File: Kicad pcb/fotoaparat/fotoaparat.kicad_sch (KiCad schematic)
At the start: 75 parts, among them IC1 Lineární Regulátor, IC3 Lineární Regulátor Displaye, J1 USB Konektor, J2 SWD, J3 LCD konektor, J4 Baterie, J5 GSD090012SEU, J6 UART, J7 Kamera, J9 Conn_01x11_Socket, U1 STM32L496RETx, U2 MCP73833-FCI/UN, Y1 8mhz krystal

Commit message: Oprava chyb
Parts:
- removed C13, C19, C20, C8: 1u, Capacitor_SMD:C_0805_2012Metric_Pad1.18x1.45mm_HandSolder, symbol Device:C
- added C22: 1u, Capacitor_SMD:C_0805_2012Metric_Pad1.18x1.45mm_HandSolder, symbol Device:C
- C7: value 1u -> 10u; footprint Capacitor_SMD:C_0805_2012Metric_Pad1.18x1.45mm_HandSolder -> Capacitor_THT:CP_Radial_D5.0mm_P2.50mm
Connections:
- net +3.3V: now also C22.2
- net GND: now also C22.1

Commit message: Připraveno na výrobu
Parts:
- added C8: 10u, Capacitor_THT:CP_Radial_D5.0mm_P2.50mm, symbol Device:C
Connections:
- net +3.3V: now also C8.1
- net GND: now also C8.2
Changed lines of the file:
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@@
 	)
 	(junction
+		(at 106.68 109.22)
+		(diameter 0)
+		(color 0 0 0 0)
+	)
+	(junction
 		(at 213.36 59.69)
 		(diameter 0)
@@
 	(wire
 		(pts
+			(xy 114.3 109.22) (xy 114.3 111.76)
+		)
+		(stroke
+			(width 0)
+			(type default)
+		)
+	)
+	(wire
+		(pts
 			(xy 207.01 20.32) (xy 207.01 19.05)
 		)
@@
 	(symbol
 		(lib_id "Device:C")
+		(at 110.49 109.22 90)
+		(unit 1)
+		(exclude_from_sim no)
+		(in_bom yes)
+		(on_board yes)
+		(dnp no)
+		(fields_autoplaced yes)
+		(property "Reference" "C8"
+			(at 110.49 101.6 90)
+			(effects
+				(font
+					(size 1.27 1.27)
+				)
+			)
+		)
+		(property "Value" "10u"
+			(at 110.49 104.14 90)
+			(effects
+				(font
+					(size 1.27 1.27)
+				)
+			)
+		)
+		(property "Footprint" "Capacitor_THT:CP_Radial_D5.0mm_P2.50mm"
+			(at 114.3 108.2548 0)
+			(effects
+				(font
+					(size 1.27 1.27)
+				)
+				(hide yes)
+			)
+		)
+		(property "Datasheet" "~"
+			(at 110.49 109.22 0)
+			(effects
+				(font
+					(size 1.27 1.27)
+				)
+				(hide yes)
+			)
+		)
+		(property "Description" "Unpolarized capacitor"
+			(at 110.49 109.22 0)
+			(effects
+				(font
+					(size 1.27 1.27)
+				)
+				(hide yes)
+			)
+		)
+		(pin "1"
+		)
+		(pin "2"
+		)
+		(instances
+			(project ""
+				(path "/af31909f-b2e8-4f24-bd61-08599f2fc290"
+					(reference "C8")
+					(unit 1)
+				)
+			)
+		)
+	)
+	(symbol
+		(lib_id "Device:C")
 		(at -77.47 172.72 270)
 		(unit 1)
@@
 					(unit 1)
 				)
+			)
+		)
+	)
+	(symbol
+		(lib_id "power:GND")
+		(at 114.3 111.76 0)
+		(unit 1)
+		(exclude_from_sim no)
+		(in_bom yes)
+		(on_board yes)
+		(dnp no)
+		(fields_autoplaced yes)
+		(property "Reference" "#PWR050"
+			(at 114.3 118.11 0)
+			(effects
+				(font
+					(size 1.27 1.27)
+				)
+				(hide yes)
+			)
+		)
+		(property "Value" "GND"
+			(at 114.3 116.84 0)
+			(effects
+				(font
+					(size 1.27 1.27)
+				)
+			)
+		)
+		(property "Footprint" ""
+			(at 114.3 111.76 0)
+			(effects
+				(font
+					(size 1.27 1.27)
+				)
+				(hide yes)
+			)
+		)
+		(property "Datasheet" ""
+			(at 114.3 111.76 0)
+			(effects
+				(font
+					(size 1.27 1.27)
+				)
+				(hide yes)
+			)
+		)
+		(property "Description" "Power symbol creates a global label with name \"GND\" , ground"
+			(at 114.3 111.76 0)
+			(effects
+				(font
+					(size 1.27 1.27)
+				)
+				(hide yes)
+			)
+		)
+		(pin "1"
+		)
+		(instances
+			(project ""
+				(path "/af31909f-b2e8-4f24-bd61-08599f2fc290"
+					(reference "#PWR050")
+					(unit 1)
+				)

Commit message: Úprava designu
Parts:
- removed C10, C11, C12, C14, C21, C9: 100n, Capacitor_SMD:C_0805_2012Metric_Pad1.18x1.45mm_HandSolder, symbol Device:C
- removed C15, C16, C22: 1u, Capacitor_SMD:C_0805_2012Metric_Pad1.18x1.45mm_HandSolder, symbol Device:C
- removed C17, C18: 30p, Capacitor_SMD:C_0805_2012Metric_Pad1.18x1.45mm_HandSolder, symbol Device:C
- removed C7, C8: 10u, Capacitor_THT:CP_Radial_D5.0mm_P2.50mm, symbol Device:C
- removed D1, D2, D3: LED, LED_SMD:LED_0805_2012Metric_Pad1.15x1.40mm_HandSolder, symbol Device:LED
- removed FB1: 120R, Inductor_SMD:L_0805_2012Metric_Pad1.05x1.20mm_HandSolder, symbol Device:FerriteBead
- removed H1, H2, H3, H4: MountingHole, MountingHole:MountingHole_3.2mm_M3, symbol Mechanical:MountingHole
- removed IC1: Lineární Regulátor, Package_TO_SOT_SMD:TSOT-23-5_HandSoldering, symbol NCP718ASN330T1G:NCP718ASN330T1G
- removed IC3: Lineární Regulátor Displaye, Package_TO_SOT_SMD:TSOT-23-5_HandSoldering, symbol NCP718ASN330T1G:NCP718ASN330T1G
- removed J1: USB Konektor, 47436:473460001, symbol 47346-0001:47346-0001
- removed J2: SWD, Connector_PinHeader_2.54mm:PinHeader_1x04_P2.54mm_Vertical, symbol Connector:Conn_01x04_Socket
- removed J3: LCD konektor, FFC2A32-20-T:GCT_FFC2A32-20-T, symbol FFC2A32-20-T:FFC2A32-20-T
- removed J4: Baterie, Connector_PinSocket_2.54mm:PinSocket_1x02_P2.54mm_Horizontal, symbol Connector:Conn_01x02_Socket
- removed J5: GSD090012SEU, gsd09:GSD090012SEU_AMP, symbol 2025-09-30_19-14-30:GSD090012SEU
- removed J6: UART, Connector_PinHeader_2.54mm:PinHeader_1x02_P2.54mm_Vertical, symbol Connector:Conn_01x02_Socket
- removed J7: Kamera, Connector_PinSocket_2.54mm:PinSocket_2x11_P2.54mm_Vertical, symbol Connector_Generic:Conn_02x11_Odd_Even
- removed J9: Conn_01x11_Socket, Connector_PinSocket_2.54mm:PinSocket_1x11_P2.54mm_Horizontal, symbol Connector:Conn_01x11_Socket
- removed R10, R11, R12, R13, R14, R15, R16, R17, R18, R19, R20, R21, R22, R23, R24, R26, R9: 4.7k, Resistor_SMD:R_0805_2012Metric_Pad1.20x1.40mm_HandSolder, symbol Device:R
- removed R25, R7: 1k, Resistor_SMD:R_0805_2012Metric_Pad1.20x1.40mm_HandSolder, symbol Device:R
- removed R8: 2, Resistor_SMD:R_0805_2012Metric_Pad1.20x1.40mm_HandSolder, symbol Device:R
- removed S1: Zapínací spínač, mfs:MFS201N24Z, symbol MFS201N-24-Z:MFS201N-24-Z
- removed S2: tlačítko doleva, mc3:MC32829, symbol MC32829:MC32829
- removed S3: prostřední tlačítko, mc3:MC32829, symbol MC32829:MC32829
- removed S4: tlačítko doprava, mc3:MC32829, symbol MC32829:MC32829
- removed S5: spínač, cfs201mb:CFS0201MB, symbol CFS-0201MB:CFS-0201MB
- removed TH1: 10k, Connector_PinSocket_2.54mm:PinSocket_1x02_P2.54mm_Horizontal, symbol Device:Thermistor
- removed U1: STM32L496RETx, Package_QFP:LQFP-64_10x10mm_P0.5mm, symbol MCU_ST_STM32L4:STM32L496RETx
- removed U2: MCP73833-FCI/UN, MCP:MSOP10_MC_MCH, symbol 2025-09-30_17-20-56:MCP73833-FCI_UN
- removed Y1: 8mhz krystal, hc4:HC49S830507030ATF, symbol HC49S-8-30-50-70-30-ATF:HC49S-8-30-50-70-30-ATF
- added J1: Conn_02x01, Connector_PinHeader_2.54mm:PinHeader_2x01_P2.54mm_Vertical, symbol Connector_Generic:Conn_02x01
- added Q1, Q2: BC547, Package_TO_SOT_THT:TO-92_Inline, symbol Transistor_BJT:BC547
- added SW1: SW_Push_Dual, Tlačítko:tlačítko 6x6x12, symbol Switch:SW_Push_Dual
- added U1: TP4056, TP4056:TP4056, symbol tp4056:tp4056
- added U2: ov7670 fifo, ov7670:ov7670, symbol ov7670:ov7670
- added U3: Stm32 Bluepill, Stm32 Bluepill:Bluepill, symbol Stm32 Bluepill:Stm32_Bluepill
- added U4: Lcd Display, Lcd Display:ili9341, symbol ili9341:lcd_ili9341
- added U5: FJ08k, Tlačítko:FJ08K-S, symbol Joystick FJ08K:FJ08k
- added U6, U8, U9: Me6211c, Package_TO_SOT_SMD:SOT-23-5, symbol Me6211c:Me6211c
- added U7: VBsemi SI2312CDS-T1-GE3, Package_TO_SOT_SMD:SOT-23W_Handsoldering, symbol Mosfet N:Mosfet_N
- BZ1: footprint Inductor_SMD:L_SXN_SMDRI73 -> Jiangsu:Jiangsu
- C1, C2, C3, C4, C5, C6: value 1u -> 4.7uf
- R1, R2: value 4.7k -> 100k; footprint Resistor_SMD:R_0805_2012Metric_Pad1.20x1.40mm_HandSolder -> Resistor_THT:R_Axial_DIN0207_L6.3mm_D2.5mm_P10.16mm_Horizontal
- R3: value 4.7k -> 10k; footprint Resistor_SMD:R_0805_2012Metric_Pad1.20x1.40mm_HandSolder -> Resistor_THT:R_Axial_DIN0207_L6.3mm_D2.5mm_P10.16mm_Horizontal
- R4: value 1k -> 100k; footprint Resistor_SMD:R_0805_2012Metric_Pad1.20x1.40mm_HandSolder -> Resistor_THT:R_Axial_DIN0207_L6.3mm_D2.5mm_P10.16mm_Horizontal
- R5: value 1k -> 30k; footprint Resistor_SMD:R_0805_2012Metric_Pad1.20x1.40mm_HandSolder -> Resistor_THT:R_Axial_DIN0207_L6.3mm_D2.5mm_P10.16mm_Horizontal
- R6: value 1k -> 50k; footprint Resistor_SMD:R_0805_2012Metric_Pad1.20x1.40mm_HandSolder -> Resistor_THT:R_Axial_DIN0207_L6.3mm_D2.5mm_P10.16mm_Horizontal
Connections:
- net +3.3V LCD is gone; now on net GND: C6.2
- net buzzer is gone; now on net +BATT: BZ1.1 (+)
- net sw2 is gone; now on an unnamed net: R2.2
- net +3.3V: now also C2.1, SW1.2, U3.23 (3v3), U5.1 (Y1), U5.4 (X1), U6.5 (Vout); no longer C4.2, R1.1, R2.1, R3.1
- net +BATT: now also R5.2, U1.5 (Bat+); no longer C2.1, C3.1, C5.1
- net GND: now also C4.2, R2.1, R3.1, R4.1, Q1.3 (E), Q2.3 (E), U1.4 (OUT-), U2.2 (gnd), U2.20 (oe), U3.19 (gnd), U3.21 (gnd), U3.22 (gnd), U4.13 (gnd), U5.2 (gnd), U5.5 (gnd), U6.2 (Vss), U6.4 (NC), U8.2 (Vss), U8.4 (NC), U9.2 (Vss), U9.4 (NC); no longer BZ1.2 (-), C4.1, C6.1
- net at R5.1: now also R4.2, U3.35 (pa1)
- net at R6.2: now also U3.9 (pa12)
- net Indikátor Nabíjení: no longer names the net of R6.1
- net Indikátor Nabíjení: now also Q1.2 (B), SW1.3
- net VBUS renamed +4V
- net +4V: now also C3.1, C5.1, U6.1 (Vin), U6.3 (CE), U7.3 (Drain), U8.1 (Vin), U8.3 (CE), U9.1 (Vin), U9.3 (CE)
- net sw1 renamed tx
- net tx: now also J1.1 (Pin_1), SW1.1, U3.6 (pa9)
- net sw3: no longer names the net of R1.2
- net sw3: now also SW1.4, U1.3 (OUT+), U7.2 (Source_gnd)
- new net: BZ1.2 (-), Q2.1 (C)
- new net: Q2.2 (B), U3.5 (pa8)
- new net: U3.28 (pb0), U4.10 (Dc)
- new net: U3.27 (pb1), U4.11 (Reset)
- new net: U3.32 (pa4), U4.12 (Cs)
- new net: U3.31 (pa5), U4.15 (sd_sck), U4.5 (T_clk), U4.8 (sck)
- new net: U3.30 (pa6), U4.16 (sd_miso), U4.2 (T_do), U4.6 (Sdo_miso)
- new net: U3.29 (pa7), U4.17 (sd_mosi), U4.3 (T_Din), U4.9 (sdi_mosi)
- new net: U3.1 (pb12), U4.18 (sd_cs)
- new net: U3.8 (pa11), U4.4 (T_cs)
- new net: U2.19 (wr), U3.10 (pa15)
- new net: U2.7 (d7), U3.11 (pb3)
- new net: U2.9 (d5), U3.12 (pb4)
- new net: U2.11 (d3), U3.13 (pb5)
- new net: U2.3 (sioc), U3.14 (pb6)
- new net: U2.4 (siod), U3.15 (pb7)
- new net: U2.13 (d1), U3.16 (pb8)
- new net: U2.8 (d6), U3.17 (pb9)
- new net: U2.14 (d0), U3.2 (pb13)
- new net: U2.10 (d4), U3.25 (pb11)
- new net: U2.12 (d2), U3.26 (pb10)
- new net: U2.18 (rck), U3.3 (pb14)
- new net: U3.33 (pa3), U5.6 (X2)
- new net: U3.34 (pa2), U5.3 (Y2)
- new net: U2.5 (vsync), U3.36 (pa0)
- new net: U2.22 (rrst), U3.4 (pb15)
- new net: Q1.1 (C), R1.1, U7.1 (Gate)
- new net +3.3V lcd: C6.1, U4.14 (Vcc), U4.7 (Led_3.3v), U9.5 (Vout)
- new net +3.3V ov7670: C4.1, U2.1 (3v3), U2.15 (rst), U8.5 (Vout)
- new net +3V3: U3.20 (3v3)
- new net -BATT: U1.6 (Bat-)
- new net rx: J1.2 (Pin_2), U2.21 (wrst), U3.7 (pa10)
- no-connect marks 35 -> 14
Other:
- note removed: "Regulátory"
- note removed: "Stm32 mikrokontrolér"

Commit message: Úprava designu
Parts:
- removed U5: FJ08k, Tlačítko:FJ08K-S, symbol Joystick FJ08K:FJ08k
- added J2: Conn_01x02_Socket, Connector_PinSocket_2.54mm:PinSocket_1x02_P2.54mm_Vertical, symbol Connector:Conn_01x02_Socket
- added Q3, Q4: BC547, Package_TO_SOT_THT:TO-92_Inline, symbol Transistor_BJT:BC547
- added R10, R7: 1k, Resistor_THT:R_Axial_DIN0207_L6.3mm_D2.5mm_P10.16mm_Horizontal, symbol Device:R
- added R8, R9: 10k, Resistor_THT:R_Axial_DIN0207_L6.3mm_D2.5mm_P10.16mm_Horizontal, symbol Device:R
- added U10, U11, U12, U5: VBsemi SI2312CDS-T1-GE3, Package_TO_SOT_SMD:SOT-23W_Handsoldering, symbol Mosfet N:Mosfet_N
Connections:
- net +3.3V: now also R10.1, R7.1
- net +4V: now also U10.2 (Source_gnd), U5.2 (Source_gnd)
- net GND: now also Q3.3 (E), Q4.3 (E), U11.2 (Source_gnd), U12.2 (Source_gnd)
- net at U3.33 (pa3): now also R9.2, U12.1 (Gate)
- net at U3.34 (pa2): now also R8.2, U11.1 (Gate)
- new net: Q4.1 (C), R10.2, U10.1 (Gate)
- new net: Q3.2 (B), R8.1
- new net: J2.2 (Pin_2), U11.3 (Drain), U12.3 (Drain)
- new net: Q4.2 (B), R9.1
- new net: J2.1 (Pin_1), U10.3 (Drain), U5.3 (Drain)
- new net: Q3.1 (C), R7.2, U5.1 (Gate)
- no-connect marks 14 -> 12

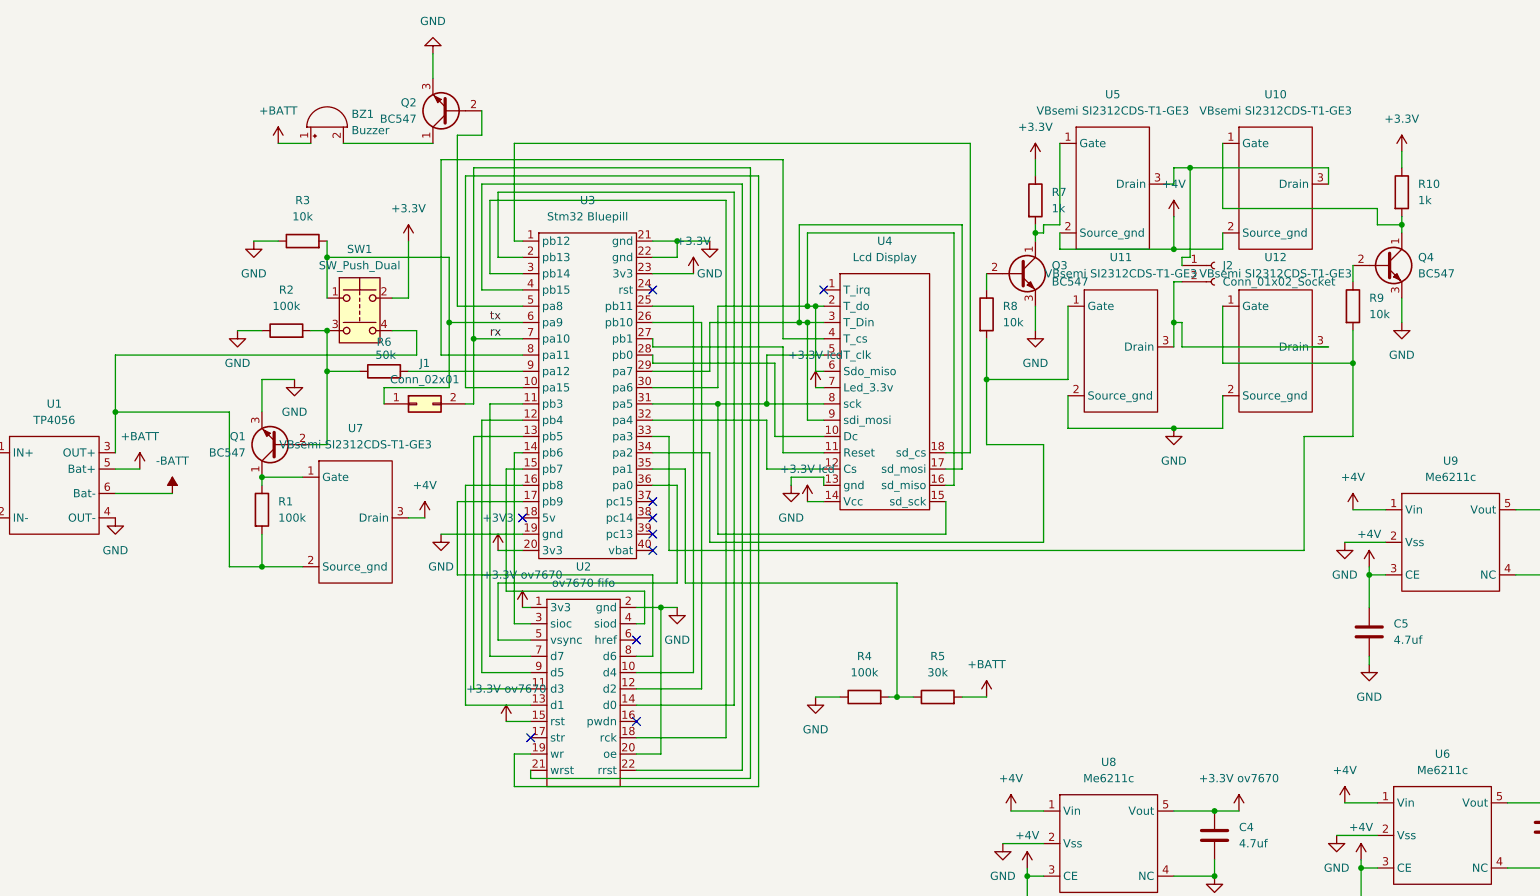
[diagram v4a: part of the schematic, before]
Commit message: Úprava schémata
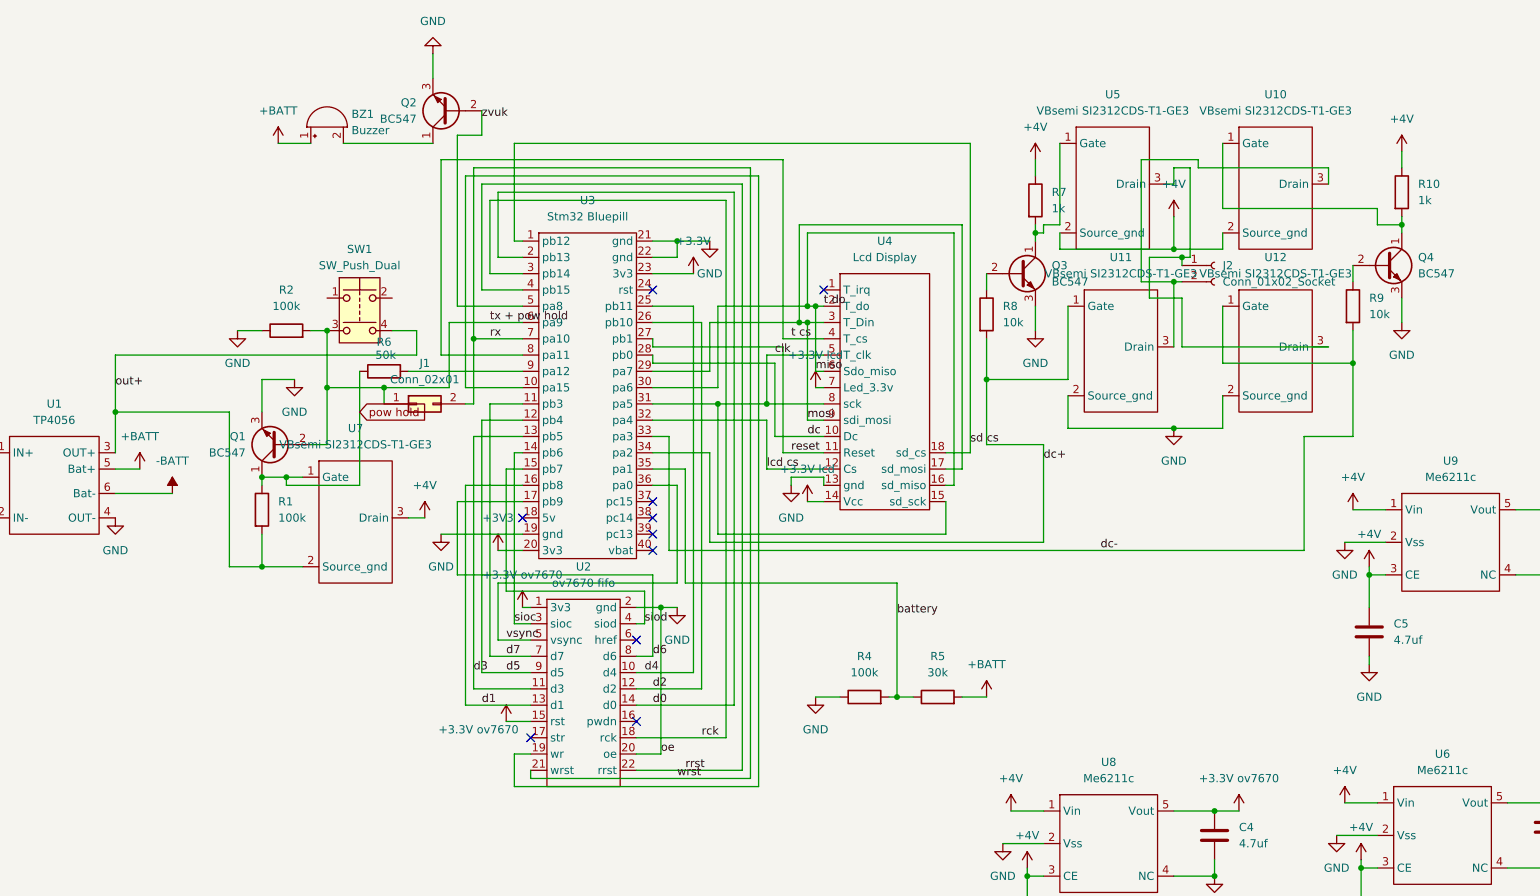
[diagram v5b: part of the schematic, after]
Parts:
- removed R3: 10k, Resistor_THT:R_Axial_DIN0207_L6.3mm_D2.5mm_P10.16mm_Horizontal, symbol Device:R
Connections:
- net +3.3V: no longer R10.1, R7.1, SW1.2
- net +4V: now also R10.1, R7.1
- net out+: now reaches R1.2, SW1.4, U1.3 (OUT+), U7.2 (Source_gnd)
- net dc+: now reaches R8.2, U11.1 (Gate), U3.34 (pa2)
- net tx + pow hold: now reaches Q1.2 (B), R2.2, SW1.3
- net tx + pow hold: now also J1.1 (Pin_1), U3.6 (pa9); no longer R6.1
- net dc-: now reaches R9.2, U12.1 (Gate), U3.33 (pa3)
- net at J2.2 (Pin_2), U11.3 (Drain): now also U10.3 (Drain); no longer U12.3 (Drain)
- net zvuk: now reaches Q2.2 (B), U3.5 (pa8)
- net dc: now reaches U3.28 (pb0), U4.10 (Dc)
- net reset: now reaches U3.27 (pb1), U4.11 (Reset)
- net lcd cs: now reaches U3.32 (pa4), U4.12 (Cs)
- net clk: now reaches U3.31 (pa5), U4.15 (sd_sck), U4.5 (T_clk), U4.8 (sck)
- net miso: now reaches U3.30 (pa6), U4.16 (sd_miso), U4.2 (T_do), U4.6 (Sdo_miso)
- net mosi: now reaches U3.29 (pa7), U4.17 (sd_mosi), U4.3 (T_Din), U4.9 (sdi_mosi)
- net sd cs: now reaches U3.1 (pb12), U4.18 (sd_cs)
- net t cs: now reaches U3.8 (pa11), U4.4 (T_cs)
- net battery: now reaches R4.2, R5.1, U3.35 (pa1)
- net at J2.1 (Pin_1), U5.3 (Drain): now also U12.3 (Drain); no longer U10.3 (Drain)
- net d7: now reaches U2.7 (d7), U3.11 (pb3)
- net d5: now reaches U2.9 (d5), U3.12 (pb4)
- net d3: now reaches U2.11 (d3), U3.13 (pb5)
- net sioc: now reaches U2.3 (sioc), U3.14 (pb6)
- net siod: now reaches U2.4 (siod), U3.15 (pb7)
- net d1: now reaches U2.13 (d1), U3.16 (pb8)
- net d6: now reaches U2.8 (d6), U3.17 (pb9)
- net d0: now reaches U2.14 (d0), U3.2 (pb13)
- net d4: now reaches U2.10 (d4), U3.25 (pb11)
- net d2: now reaches U2.12 (d2), U3.26 (pb10)
- net rck: now reaches U2.18 (rck), U3.3 (pb14)
- net vsync: now reaches U2.5 (vsync), U3.36 (pa0)
- net rrst: now reaches U2.22 (rrst), U3.4 (pb15)
- net pow hold: now reaches Q1.1 (C), R1.1, U7.1 (Gate)
- net pow hold: now also R6.1
- removed net tx: J1.1 (Pin_1), SW1.1, U3.6 (pa9)

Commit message: Resistory
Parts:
- added R11, R12: 1k, Resistor_THT:R_Axial_DIN0207_L6.3mm_D2.5mm_P10.16mm_Horizontal, symbol Device:R
- added R3: 100, Resistor_THT:R_Axial_DIN0207_L6.3mm_D2.5mm_P10.16mm_Horizontal, symbol Device:R
- R2: value 100k -> 50k
- R6: value 50k -> 1k
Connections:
- net GND: no longer U6.4 (NC), U8.4 (NC), U9.4 (NC)
- net pow hold: now also R6.2, U3.9 (pa12)
- net tx + pow hold: now also R12.2; no longer Q1.2 (B)
- net zvuk: now also R11.1; no longer Q2.2 (B)
- net at Q2.1 (C): now also R3.2; no longer BZ1.2 (-)
- net wr: now reaches U2.19 (wr), U3.10 (pa15)
- new net: Q1.2 (B), R12.1
- new net: Q2.2 (B), R11.2
- new net: BZ1.2 (-), R3.1
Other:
- moved on the sheet: BZ1

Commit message: Menší deska a větší plošky pro pájení
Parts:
- added H1, H2, H3, H4: MountingHole, MountingHole:MountingHole_3.2mm_M3, symbol Mechanical:MountingHole
- J1: footprint Connector_PinHeader_2.54mm:PinHeader_2x01_P2.54mm_Vertical -> txrx:txrx
- J2: footprint Connector_PinSocket_2.54mm:PinSocket_1x02_P2.54mm_Vertical -> txrx:txrx
- Q1, Q2, Q3, Q4: footprint Package_TO_SOT_THT:TO-92_Inline -> transistor:npnTHT
- R1, R10, R11, R12, R2, R3, R4, R5, R6, R7, R8, R9: footprint Resistor_THT:R_Axial_DIN0207_L6.3mm_D2.5mm_P10.16mm_Horizontal -> resistorTHT:thtRESISTOR
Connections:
- net GND: now also U6.4 (NC), U8.4 (NC), U9.4 (NC)
- net pow hold: no longer R6.2, U3.9 (pa12)
- new net pow hold mcu: R6.2, U3.9 (pa12)

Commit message: Úprava dps
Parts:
- added C7, C8, C9: 4.7uf, Capacitor_THT:CP_Radial_D5.0mm_P2.00mm, symbol Device:C
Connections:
- net +3.3V: now also C8.1
- net +3.3V lcd: now also C9.1
- net +3.3V ov7670: now also C7.1
- net GND: now also C7.2, C8.2, C9.2
